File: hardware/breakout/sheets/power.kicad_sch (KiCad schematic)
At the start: 63 parts, among them J1 M12A_5, J52 Chassis fan 1, J53 Chassis fan 2, J54 Chassis fan 3, J55 Chassis fan 4, J56 Chassis earth stud, U1 LD1117S33TR_SOT223, U2 IH1215D, U3 TPS7A4901, U4 TPS7A3001

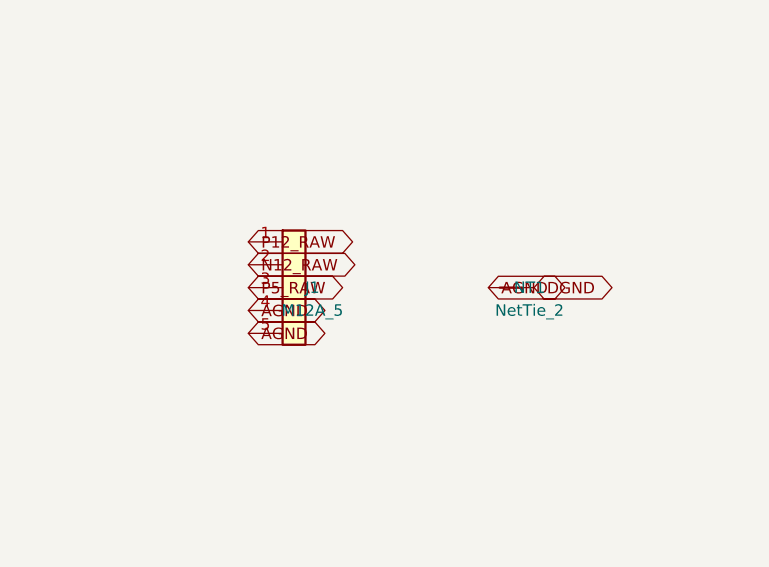
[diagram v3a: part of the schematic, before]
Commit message: fix(hardware): rebuild the connectors on their primary drawings (F6, R1, D3)
Audit step 5, the mechanical half. Three connectors changed, one of them a
fab-stopper, and none of it was visible to the netlist.

MDR68 (the fab-stopper). Rebuilt from MH drawing 3700-0121-01 rev 3.0. The
as-built footprint drilled contacts at 0.5 mm against a required 0.85 mm -- the
pins do not fit, so the board could not have been assembled -- and laid them out
as 2 rows at 2.84 mm where the drawing shows 4 staggered rows of 17 at 1.905 mm.
The 4-row stagger is what makes an 0.85 mm drill manufacturable at a 1.27 mm
mating pitch at all; the array now spans the drawing's own 41.91 mm exactly,
which is the arithmetic that confirms the reading. The claim made during the
audit that it had "no mounting holes at all" was wrong: it had two, Ø2.79 on
57.9 mm centres against the drawing's Ø2.77 on 57.93.

M12 (ruling R1). M12A_5_Panel is deleted, symbol and footprint and generator
function alike. Its contact geometry was sourced well -- IEC 61076-2-101
A-coding, cross-checked three ways -- and it made no difference, because the part
the design procures (Phoenix 1551833) terminates in AWG 22-20 wire and mounts
through the panel. It has no PCB tails, so no board-mount footprint of any
dimensions could have been right, and as built every cable insertion and every
3-4 N.m tightening loaded PCB pads directly. J1 is now a stock 5-way header where
those flying leads land; the connector stays in the order BOM as chassis
furniture.

BNC (F6). BNC_PanelMountable_Vertical puts the connector axis perpendicular to
the PCB -- a 9.65 mm barrel hole through the board -- so on a 430x240 mm board
lying flat in a 2U chassis all 31 barrels pointed at the lid rather than at the
panels. It also cost 5,654 mm2 of pad and 2,267 mm2 of removed copper on every
layer. Replaced by a right-angle dual jack built from Amphenol drawing 31-6575
rev A: 31 ports on 17 bodies, 3 spare ports, every shell still routed
individually.
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
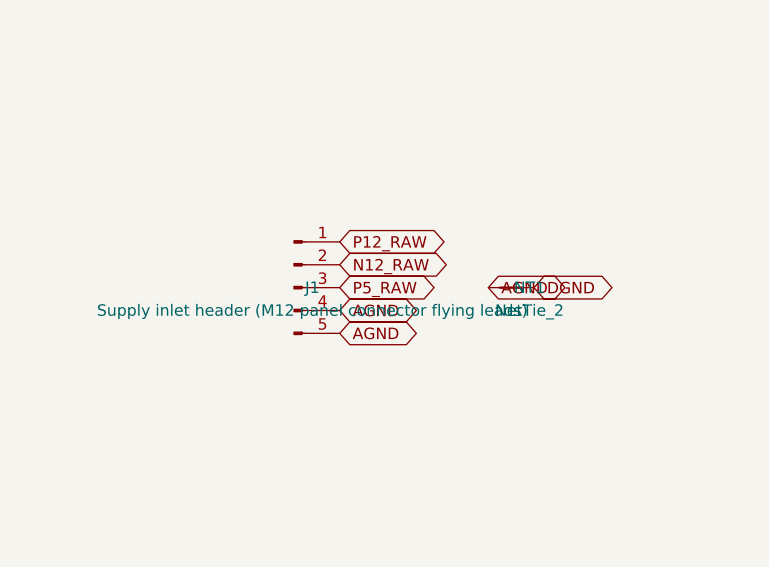
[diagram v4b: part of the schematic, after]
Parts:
- removed J1: M12A_5, wl-sync:M12A_5_Panel, symbol wl-sync:M12A_5
- added J1: Supply inlet header (M12 panel connector flying l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, Connector_PinHeader_2.54mm:PinHeader_1x05_P2.54mm_Vertical, symbol Connector:Conn_01x05_Pin
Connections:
- net AGND: now also J1.4 (Pin_4), J1.5 (Pin_5)
- net N12_RAW: now also J1.2 (Pin_2)
- net P12_RAW: now also J1.1 (Pin_1)
- net P5_RAW: now also J1.3 (Pin_3)
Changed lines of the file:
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@@
 	(paper "A2")
 	(symbol
-		(lib_id "wl-sync:M12A_5")
+		(lib_id "Connector:Conn_01x05_Pin")
 		(at 20.32 95.25 0)
 		(unit 1)
@@
 			(effects (font (size 1.27 1.27)))
 		)
-		(property "Value" "M12A_5"
+		(property "Value" "Supply inlet header (M12 panel connector flying leads)"
 			(at 22.352 97.79 0)
 			(effects (font (size 1.27 1.27)))
 		)
-		(property "Footprint" "wl-sync:M12A_5_Panel"
+		(property "Footprint" "Connector_PinHeader_2.54mm:PinHeader_1x05_P2.54mm_Vertical"
 			(at 20.32 95.25 0)
 			(effects (font (size 1.27 1.27)) (hide yes))
@@
 	(global_label "P12_RAW"
 		(shape bidirectional)
-		(at 15.24 90.17 0)
+		(at 25.4 90.17 0)
 		(effects (font (size 1.27 1.27)) (justify left))
 		(property "Intersheetrefs" "${INTERSHEET_REFS}"
-			(at 15.24 90.17 0)
+			(at 25.4 90.17 0)
 			(effects (font (size 1.27 1.27)) (hide yes))
 		)
@@
 	(global_label "N12_RAW"
 		(shape bidirectional)
-		(at 15.24 92.71 0)
+		(at 25.4 92.71 0)
 		(effects (font (size 1.27 1.27)) (justify left))
 		(property "Intersheetrefs" "${INTERSHEET_REFS}"
-			(at 15.24 92.71 0)
+			(at 25.4 92.71 0)
 			(effects (font (size 1.27 1.27)) (hide yes))
 		)
@@
 	(global_label "P5_RAW"
 		(shape bidirectional)
-		(at 15.24 95.25 0)
+		(at 25.4 95.25 0)
 		(effects (font (size 1.27 1.27)) (justify left))
 		(property "Intersheetrefs" "${INTERSHEET_REFS}"
-			(at 15.24 95.25 0)
+			(at 25.4 95.25 0)
 			(effects (font (size 1.27 1.27)) (hide yes))
 		)
@@
 	(global_label "AGND"
 		(shape bidirectional)
-		(at 15.24 97.79 0)
+		(at 25.4 97.79 0)
 		(effects (font (size 1.27 1.27)) (justify left))
 		(property "Intersheetrefs" "${INTERSHEET_REFS}"
-			(at 15.24 97.79 0)
+			(at 25.4 97.79 0)
 			(effects (font (size 1.27 1.27)) (hide yes))
 		)
@@
 	(global_label "AGND"
 		(shape bidirectional)
-		(at 15.24 100.33 0)
+		(at 25.4 100.33 0)
 		(effects (font (size 1.27 1.27)) (justify left))
 		(property "Intersheetrefs" "${INTERSHEET_REFS}"
-			(at 15.24 100.33 0)
+			(at 25.4 100.33 0)
 			(effects (font (size 1.27 1.27)) (hide yes))
 		)
